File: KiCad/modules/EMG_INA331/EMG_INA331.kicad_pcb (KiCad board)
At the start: 4 copper layers, 15 x 11 mm, 35 parts, among them J1 Conn_01x01_Pin, J10 Conn_01x01_Pin, J11 Conn_01x01_Pin, J12 Conn_01x01_Pin, J13 Conn_01x01_Pin, J14 Conn_01x01_Pin, J7 Conn_01x01_Pin, J9 Conn_01x01_Pin, U1 TLV9044IPWR, U2 AP2112K-3.3TRG1, U3 INA350ABSIDSGR_C4370677

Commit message: INA331 IMUICM
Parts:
- removed J11, J12, J13, J14: Conn_01x01_Pin, Connector_PinHeader_1.27mm:PinHeader_1x01_P1.27mm_Vertical
- removed R14: R, Resistor_SMD:R_0201_0603Metric
- removed kibuzzard-658D7E24: G***, kibuzzard-658D7E24
- added C13: 1uF, Capacitor_SMD:C_0402_1005Metric, B.Cu at (36.0, 37.5)
- added C15: 1u, Capacitor_SMD:C_0402_1005Metric, B.Cu at (36.0, 35.5)
- added C2: 100nF, Capacitor_SMD:C_0402_1005Metric, F.Cu at (28.7, 32.7)
- added C7: 1uF, Capacitor_SMD:C_0402_1005Metric, B.Cu at (24.3, 38.0)
- added J2: Conn_01x01_Pin, 00_custom-footprints:PinHeader_1x01_P1.27mm_Vertical, F.Cu at (26.8, 30.0)
- added J3: Conn_01x01_Pin, 00_custom-footprints:PinHeader_1x01_P1.27mm_Vertical, F.Cu at (28.1, 30.0)
- added J4: Conn_01x01_Pin, 00_custom-footprints:PinHeader_1x01_P1.27mm_Vertical, F.Cu at (29.4, 30.0)
- added J5: Conn_01x01_Pin, 00_custom-footprints:PinHeader_1x01_P1.27mm_Vertical, F.Cu at (30.6, 30.0)
- added J6: Conn_01x01_Pin, 00_custom-footprints:PinHeader_1x01_P1.27mm_Vertical, F.Cu at (31.9, 30.0)
- added J8: Conn_01x01_Pin, 00_custom-footprints:PinHeader_1x01_P1.27mm_Vertical, F.Cu at (34.4, 30.0)
- added R8: 100k, Resistor_SMD:R_0402_1005Metric, F.Cu at (26.1, 36.5)
- added TP1: TestPoint, 00_custom-footprints:TestPoint_Pad_D1.0mm, B.Cu at (36.2, 33.0)
- added TP2: TestPoint, 00_custom-footprints:TestPoint_Pad_D1.0mm, B.Cu at (36.2, 31.2)
- added TP3: TestPoint, 00_custom-footprints:TestPoint_Pad_D1.0mm, B.Cu at (31.0, 37.2)
- added U4: OPA333, 00_lcsc:SOT-23-5_L2.9-W1.6-P0.95-LS2.8-BR, F.Cu at (33.5, 37.4)
- added U5: CJ432, 00_lcsc:SOT-23-3_L2.9-W1.3-P1.90-LS2.4-BR, F.Cu at (30.7, 33.9)
- added U6: LIS3DHTR, 00_lcsc:LGA-16_L3.0-W3.0-P0.50-TL, F.Cu at (34.7, 33.3)
- added kibuzzard-6606B2BA: G***, kibuzzard-6606B2BA, B.Cu at (29.5, 32.6)
- C1: value 1uF -> 10uF
- C11, C6: moved to B.Cu
- C12, C9: value 1uF -> 100nF; moved to B.Cu
- C14: value 1uF -> 100n; moved to B.Cu
- C3: value 1uF -> 10nF
- C4, C5: value 1uF -> 100pF; moved to B.Cu
- C8: footprint Capacitor_SMD:C_0201_0603Metric -> Capacitor_SMD:C_0402_1005Metric
- J1, J10, J7, J9: footprint Connector_PinHeader_1.27mm:PinHeader_1x01_P1.27mm_Vertical -> 00_custom-footprints:PinHeader_1x01_P1.27mm_Vertical
- R1: value R -> 2k; footprint Resistor_SMD:R_0201_0603Metric -> Resistor_SMD:R_0402_1005Metric; moved to B.Cu
- R10, R12: value R -> 1k; footprint Resistor_SMD:R_0201_0603Metric -> Resistor_SMD:R_0402_1005Metric
- R11: value R -> 100k; footprint Resistor_SMD:R_0201_0603Metric -> Resistor_SMD:R_0402_1005Metric; moved to B.Cu
- R2, R6, R7: value R -> 10k; footprint Resistor_SMD:R_0201_0603Metric -> Resistor_SMD:R_0402_1005Metric; moved to B.Cu
- R3: value R -> 330; footprint Resistor_SMD:R_0201_0603Metric -> Resistor_SMD:R_0402_1005Metric
- R4, R5: value R -> 4k; footprint Resistor_SMD:R_0201_0603Metric -> Resistor_SMD:R_0402_1005Metric
- R9: value R -> 1M; footprint Resistor_SMD:R_0201_0603Metric -> Resistor_SMD:R_0402_1005Metric
- U1: value TLV9044IPWR -> INA350ABSIDSGR; footprint 00_lcsc:TSSOP-14_L5.0-W4.4-P0.65-LS6.4-BL -> 00_lcsc:WSON-8_L2.0-W2.0-P0.50-TL-EP
- U2: value AP2112K-3.3TRG1 -> OPA333; footprint 00_Custom:SOT95P285X140-5N -> 00_lcsc:SOT-23-5_L2.9-W1.6-P0.95-LS2.8-BR; moved to B.Cu
- U3: value INA350ABSIDSGR_C4370677 -> AP2112K-3.3TRG1; footprint 00_lcsc:WSON-8_L2.0-W2.0-P0.50-TL-EP -> 00_lcsc:SOT-25-5_L2.9-W1.6-P0.95-LS2.8-BL
- moved R2 40.4 mm to (33.6, 35.4)
- moved R1 37.7 mm to (30.6, 35.3)
- moved R12 37.2 mm to (35.8, 37.9), turned to 90 degrees
- moved R11 36.6 mm to (36.0, 38.5)
- moved R5 36.5 mm to (30.0, 38.4), turned to 180 degrees
- moved R3 33.9 mm to (27.6, 32.0), turned to -90 degrees
- moved C14 31.9 mm to (36.0, 36.5), turned to 180 degrees
- moved R10 31.4 mm to (30.4, 36.4)
- moved R4 31.3 mm to (28.0, 38.6), turned to 180 degrees
- moved R7 31.3 mm to (23.8, 36.3), turned to 90 degrees
- moved R6 31.1 mm to (24.8, 36.3), turned to -90 degrees
- moved C12 29.6 mm to (33.6, 36.4)
- moved R9 29.1 mm to (28.1, 35.2)
- moved C6 27.7 mm to (23.8, 32.9), turned to 90 degrees
- moved U3 26.1 mm to (25.0, 32.4), turned to -90 degrees
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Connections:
- C1 pad 1: unconnected-(C1-Pad1) -> Vref
- C1 pad 2: unconnected-(C1-Pad2) -> GND
- C10 pad 1: unconnected-(C10-Pad1) -> /OUT_INA
- C10 pad 2: unconnected-(C10-Pad2) -> Net-(U4-+IN)
- C11 pad 1: unconnected-(C11-Pad1) -> +3.3VA
- C11 pad 2: unconnected-(C11-Pad2) -> GND
- C12 pad 1: unconnected-(C12-Pad1) -> +3.3VA
- C12 pad 2: unconnected-(C12-Pad2) -> GND
- C14 pad 1: unconnected-(C14-Pad1) -> +3.3V
- C14 pad 2: unconnected-(C14-Pad2) -> GND
- C3 pad 1: unconnected-(C3-Pad1) -> /IN+
- C3 pad 2: unconnected-(C3-Pad2) -> /IN-
- C4 pad 1: unconnected-(C4-Pad1) -> /IN+
- C4 pad 2: unconnected-(C4-Pad2) -> Vref
- C5 pad 1: unconnected-(C5-Pad1) -> Vref
- C5 pad 2: unconnected-(C5-Pad2) -> /IN-
- C6 pad 1: unconnected-(C6-Pad1) -> +3.3V
- C6 pad 2: unconnected-(C6-Pad2) -> GND
- C8 pad 1: +3.3VA -> /REF
- C8 pad 2: GND -> Net-(U2--IN)
- C9 pad 1: +3.3V -> +3.3VA
- J1 pad 1: unconnected-(J1-Pin_1-Pad1) -> +3.3V
- J10 pad 1: /MOSI -> /PROB+
- J7 pad 1: /extRef -> /CSB
- J9 pad 1: /MISO -> /PROB-
- R1 pad 1: unconnected-(R1-Pad1) -> Vref
- R1 pad 2: unconnected-(R1-Pad2) -> Net-(U5-R)
- R10 pad 1: unconnected-(R10-Pad1) -> Vref
- R10 pad 2: unconnected-(R10-Pad2) -> Net-(U4--IN)
- R11 pad 1: unconnected-(R11-Pad1) -> Net-(U4--IN)
- R11 pad 2: unconnected-(R11-Pad2) -> /OUT1
- R12 pad 1: unconnected-(R12-Pad1) -> /OUT1
- R12 pad 2: unconnected-(R12-Pad2) -> GND
- R2 pad 1: unconnected-(R2-Pad1) -> Net-(U5-R)
- R2 pad 2: unconnected-(R2-Pad2) -> GND
- R3 pad 1: unconnected-(R3-Pad1) -> +3.3VA
- R3 pad 2: unconnected-(R3-Pad2) -> Vref
- R4 pad 1: unconnected-(R4-Pad1) -> /PROB+
- R4 pad 2: unconnected-(R4-Pad2) -> /IN+
- R5 pad 1: unconnected-(R5-Pad1) -> /PROB-
- R5 pad 2: unconnected-(R5-Pad2) -> /IN-
- R6 pad 1: unconnected-(R6-Pad1) -> /REF
- R6 pad 2: unconnected-(R6-Pad2) -> Net-(U1-GS)
- R7 pad 1: unconnected-(R7-Pad1) -> Net-(U1-GS)
- R7 pad 2: unconnected-(R7-Pad2) -> /OUT_INA
- R9 pad 1: unconnected-(R9-Pad1) -> Net-(U4-+IN)
- R9 pad 2: unconnected-(R9-Pad2) -> Vref
- U1 pad 1: unconnected-(U1-OUT1-Pad1) -> Net-(U1-GS)
- U1 pad 2: unconnected-(U1-IN1--Pad2) -> /IN+
- U1 pad 3: unconnected-(U1-IN1+-Pad3) -> /IN-
- U1 pad 4: unconnected-(U1-VCC+-Pad4) -> GND
- U1 pad 5: unconnected-(U1-IN2+-Pad5) -> /REF
- U1 pad 6: unconnected-(U1-IN2--Pad6) -> /OUT_INA
- U1 pad 7: unconnected-(U1-OUT2-Pad7) -> +3.3VA
- U2 pad 1: +3.3V -> /REF
- U2 pad 2: GND -> +3.3VA
- U2 pad 3: +3.3V -> Vref
- U2 pad 4: (no net) -> Net-(U2--IN)
- U2 pad 5: +3.3VA -> GND
- U3 pad 1: unconnected-(U3-GS-Pad1) -> +3.3V
- U3 pad 2: unconnected-(U3-IN–-Pad2) -> GND
- U3 pad 3: unconnected-(U3-IN+-Pad3) -> +3.3V
- U3 pad 5: unconnected-(U3-REF-Pad5) -> +3.3VA
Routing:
- net (no net): track 51.8 -> 0.00 mm, vias 3 -> 0
- net +3.3VA: track 5.52 -> 39.6 mm, vias 0 -> 1
- net +3.3V: track 14.8 -> 32.3 mm, vias 0 -> 1
- net Vref: track 0.00 -> 16.0 mm, vias 0 -> 2
- net Net-(U4-+IN): track 0.00 -> 12.0 mm
- net /OUT1: track 0.00 -> 11.7 mm, vias 0 -> 2
- net /extRef: track 8.96 -> 0.00 mm
- net /IN-: track 0.00 -> 8.06 mm, vias 0 -> 1
- net /REF: track 0.00 -> 7.22 mm, vias 0 -> 2
- net Net-(U4--IN): track 0.00 -> 6.78 mm, vias 0 -> 1
- net /IN+: track 0.00 -> 5.94 mm, vias 0 -> 1
- net Net-(U5-R): track 0.00 -> 5.61 mm, vias 0 -> 1
- net /ADC2: track 0.00 -> 5.49 mm, vias 0 -> 1
- net /OUT_INA: track 0.00 -> 5.31 mm, vias 0 -> 1
- net /SCLK: track 2.51 -> 7.14 mm
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- added copper zone on F.Cu, net Vref
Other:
- board text added: "Aightech"
- board text removed: "by Aightech"

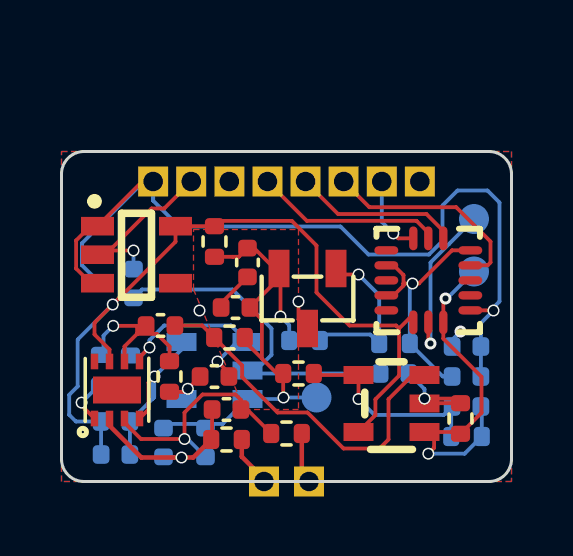
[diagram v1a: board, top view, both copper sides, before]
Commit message: refactor and fixing most of the modules
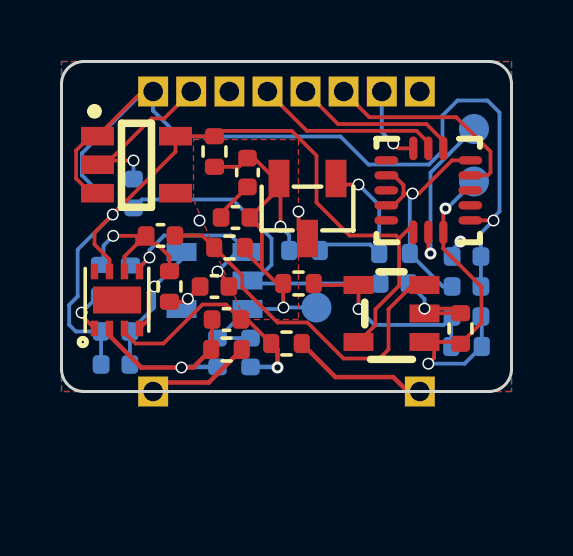
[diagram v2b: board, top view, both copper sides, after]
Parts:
- moved J10 4.76 mm to (25.6, 37.0)
- moved J9 4.76 mm to (34.4, 37.0)
- moved C4 3.50 mm to (27.7, 35.7)
- moved C5 3.35 mm to (28.8, 35.7)
- moved C1 3.00 mm to (28.3, 31.2)
- moved C2 3.00 mm to (28.7, 29.7)
- moved C11 3.00 mm to (24.9, 30.4)
- moved C12 3.00 mm to (33.6, 33.4)
- moved C13 3.00 mm to (36.0, 34.5)
- moved C14 3.00 mm to (36.0, 33.5)
- moved C15 3.00 mm to (36.0, 32.5)
- moved C3 3.00 mm to (28.0, 34.6)
- moved C6 3.00 mm to (23.8, 29.9)
- moved C7 3.00 mm to (24.3, 35.0)
- moved C8 3.00 mm to (27.6, 33.5)
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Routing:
- net /PROB-: track 1.52 -> 4.56 mm
- net /PROB+: track 1.62 -> 3.41 mm
- net Vref: track 16.0 -> 15.3 mm
- net /IN+: track 5.94 -> 6.54 mm

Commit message: cleaned all modules + production files
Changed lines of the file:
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@@
 		(sheetname "Root")
 		(sheetfile "EMG_INA331.kicad_sch")
-		(attr through_hole exclude_from_pos_files)
+		(attr through_hole exclude_from_pos_files exclude_from_bom dnp)
 		(fp_line
 			(start -1.05 -0.11)
@@
 			(size 1 1)
 			(drill 0.65)
+			(property pad_prop_castellated)
 			(layers "*.Cu" "*.Mask")
 			(remove_unused_layers no)
@@
 		(sheetname "Root")
 		(sheetfile "EMG_INA331.kicad_sch")
-		(attr through_hole exclude_from_pos_files)
+		(attr through_hole exclude_from_pos_files exclude_from_bom dnp)
 		(fp_line
 			(start -1.05 -0.11)
@@
 			(size 1 1)
 			(drill 0.65)
+			(property pad_prop_castellated)
 			(layers "*.Cu" "*.Mask")
 			(remove_unused_layers no)
@@
 		(at 35.8 32)
 		(size 0.4)
-		(drill 0.2)
+		(drill 0.3)
 		(layers "F.Cu" "B.Cu")
 		(net 1)
@@
 		(at 29.7 36.2)
 		(size 0.4)
-		(drill 0.2)
+		(drill 0.3)
 		(layers "F.Cu" "B.Cu")
 		(net 19)
@@
 		(at 35.3 30.9)
 		(size 0.4)
-		(drill 0.2)
+		(drill 0.3)
 		(layers "F.Cu" "B.Cu")
 		(net 22)
@@
 		(at 34.8 32.4)
 		(size 0.4)
-		(drill 0.2)
+		(drill 0.3)
 		(layers "F.Cu" "B.Cu")
 		(net 29)
